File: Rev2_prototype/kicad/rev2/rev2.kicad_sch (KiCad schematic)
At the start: 9 parts, among them M1 Motor_Servo, SW1 SW_Push, SW2 SW_Push

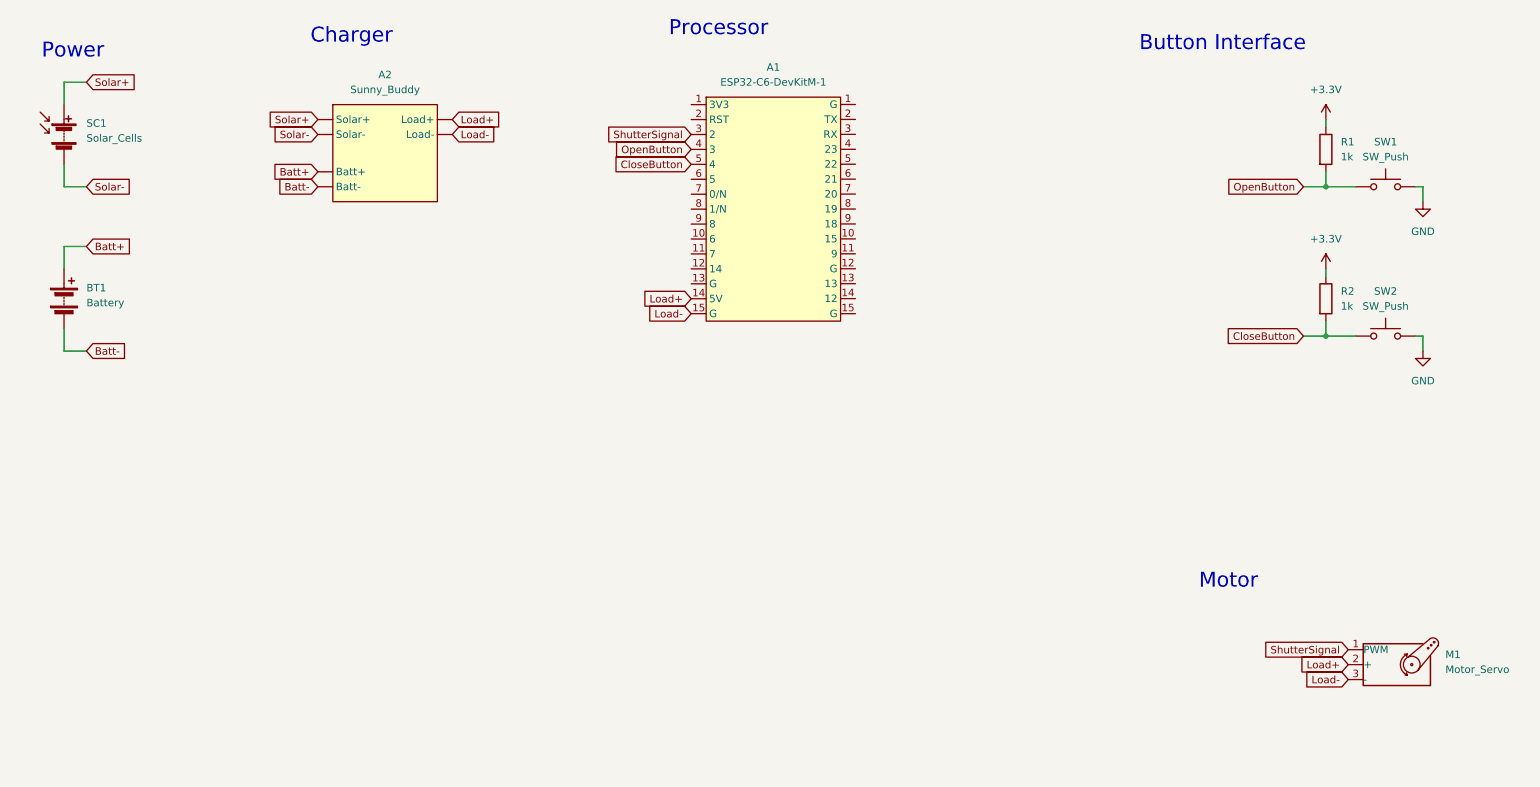
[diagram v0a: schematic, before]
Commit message: Add battery voltage sensing circuit
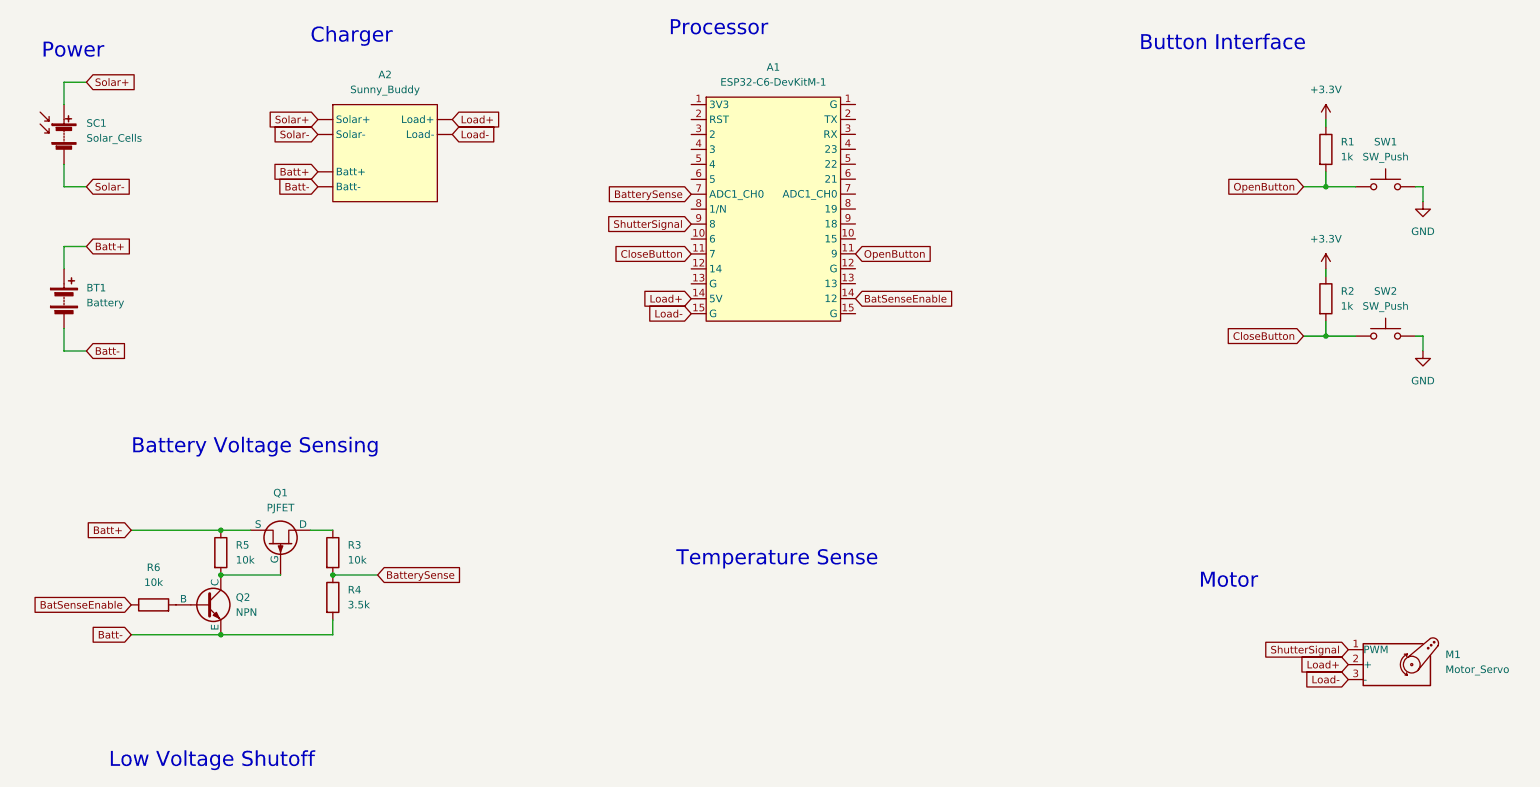
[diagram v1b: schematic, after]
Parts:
- added Q1: PJFET, symbol Simulation_SPICE:PJFET
- added Q2: NPN, symbol Simulation_SPICE:NPN
- added R3, R5, R6: 10k, symbol Device:R
- added R4: 3.5k, symbol Device:R
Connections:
- net Batt+: now also Q1.3 (S), R5.1
- net Batt-: now also Q2.3 (E), R4.2
- net CloseButton: now also A1.11 (9); no longer A1.5 (4)
- net OpenButton: no longer A1.4 (3)
- net ShutterSignal: now also A1.9 (8); no longer A1.3 (RX)
- net BatterySense: now reaches A1.7 (20)
- net BatterySense: now also R3.2, R4.1
- new net: Q1.2 (G), Q2.1 (C), R5.2
- new net: Q2.2 (B), R6.2
- new net: Q1.1 (D), R3.1
- new net BatSenseEnable: R6.1
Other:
- note added: "Battery Voltage Sensing"
- note added: "Low Voltage Shutoff"
- note added: "Temperature Sense"

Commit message: Changes idk
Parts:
- removed Q1: PJFET, symbol Simulation_SPICE:PJFET
- added Q1: ZXMP4A16G, Package_TO_SOT_SMD:SOT-223-3_TabPin2, symbol Transistor_FET:ZXMP4A16G
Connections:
- net Batt+: now also Q1.3 (S)
- net at Q2.1 (C), R5.2: now also Q1.1 (G)
- net at R3.1: now also Q1.2 (D)
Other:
- note removed: "Low Voltage Shutoff"
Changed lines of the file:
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@@
-    (effects (font (size 2.54 2.54)) (justify left bottom))
-  )
-  (text "Low Voltage Shutoff" (at 38.1 152.4 0)
     (effects (font (size 2.54 2.54)) (justify left bottom))
   )
@@
     (pin "5")
     (pin "1")
-    (pin "7")
+    (pin "7" (alternate "ADC1_CH0"))
     (pin "8")
     (pin "2")
@@
     )
   )
+  (symbol (lib_id "Transistor_FET:ZXMP4A16G") (at 67.31 114.3 270) (mirror x) (unit 1)
+    (in_bom yes) (on_board yes) (dnp no)
+    (property "Reference" "Q1" (at 67.31 105.41 90)
+      (effects (font (size 1.27 1.27)))
+    )
+    (property "Value" "ZXMP4A16G" (at 67.31 107.95 90)
+      (effects (font (size 1.27 1.27)))
+    )
+    (property "Footprint" "Package_TO_SOT_SMD:SOT-223-3_TabPin2" (at 65.405 109.22 0)
+      (effects (font (size 1.27 1.27) italic) (justify left) hide)
+    )
+    (property "Datasheet" "https://www.diodes.com/assets/Datasheets/ZXMP4A16G.pdf" (at 63.5 109.22 0)
+      (effects (font (size 1.27 1.27)) (justify left) hide)
+    )
+    (pin "2")
+    (pin "1")
+    (pin "3")
+    (instances
+      (project "rev2"
+        (path "/b183557f-a9cf-458d-96f7-90bf56cd176b"
+          (reference "Q1") (unit 1)
+        )
+      )
+    )
+  )
   (symbol (lib_id "power:+3.3V") (at 245.11 41.91 0) (unit 1)
     (in_bom yes) (on_board yes) (dnp no) (fields_autoplaced)
@@
         )
       )
-    )
-  )
-  (symbol (lib_id "Simulation_SPICE:PJFET") (at 67.31 114.3 270) (mirror x) (unit 1)
-    (in_bom yes) (on_board yes) (dnp no) (fields_autoplaced)
-    (property "Reference" "Q1" (at 67.31 105.41 90)
-      (effects (font (size 1.27 1.27)))
-    )
-    (property "Value" "PJFET" (at 67.31 107.95 90)
-      (effects (font (size 1.27 1.27)))
-    )
-    (property "Footprint" "" (at 69.85 109.22 0)
-      (effects (font (size 1.27 1.27)) hide)
-    )
-    (property "Datasheet" "~" (at 67.31 114.3 0)
-      (effects (font (size 1.27 1.27)) hide)
-    )
-    (property "Sim.Device" "PJFET" (at 67.31 114.3 0)
-      (effects (font (size 1.27 1.27)) hide)
-    )
-    (property "Sim.Type" "SHICHMANHODGES" (at 67.31 114.3 0)
-      (effects (font (size 1.27 1.27)) hide)
-    )
-    (property "Sim.Pins" "1=D 2=G 3=S" (at 67.31 114.3 0)
-      (effects (font (size 1.27 1.27)) hide)
-    )
-    (pin "2")
-    (pin "3")
-    (pin "1")
-    (instances
-      (project "rev2"
-        (path "/b183557f-a9cf-458d-96f7-90bf56cd176b"
-          (reference "Q1") (unit 1)
-        )
-      )
